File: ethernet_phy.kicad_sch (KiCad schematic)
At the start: 24 parts, among them J2 RJ45_Abracon_ARJP11A-MASA-B-A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, U1 RTL8201F

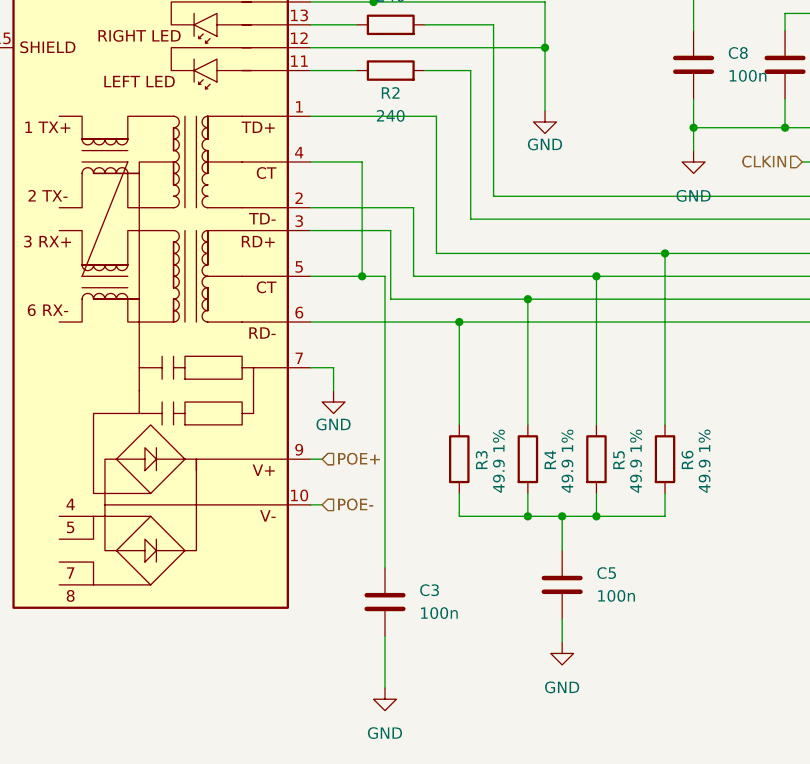
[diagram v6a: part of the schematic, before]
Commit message: RT9400 module option added
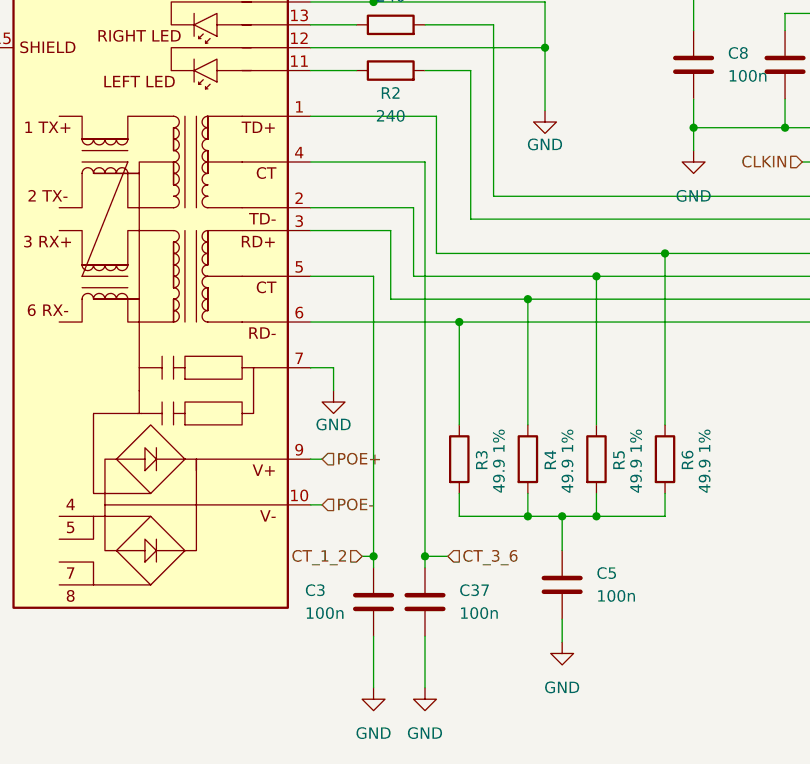
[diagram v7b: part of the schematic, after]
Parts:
- added C37: 100n, Capacitor_SMD:C_0603_1608Metric_Pad1.08x0.95mm_HandSolder, symbol Device:C
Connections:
- net GND: now also C37.2
- net CT_1_2: now reaches C3.1, J2.5 (CT)
- net CT_1_2: no longer J2.4 (CT)
- new net CT_3_6: C37.1, J2.4 (CT)
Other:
- moved on the sheet: C3
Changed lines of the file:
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@@
   (junction (at 92.075 48.26) (diameter 0) (color 0 0 0 0)
   )
+  (junction (at 92.075 128.905) (diameter 0) (color 0 0 0 0)
+  )
   (junction (at 111.125 124.46) (diameter 0) (color 0 0 0 0)
   )
@@
   (junction (at 118.745 48.26) (diameter 0) (color 0 0 0 0)
   )
+  (junction (at 86.36 128.905) (diameter 0) (color 0 0 0 0)
+  )
   (junction (at 107.315 124.46) (diameter 0) (color 0 0 0 0)
   )
@@
   (junction (at 134.62 40.005) (diameter 0) (color 0 0 0 0)
   )
-  (junction (at 85.09 97.79) (diameter 0) (color 0 0 0 0)
-  )
   (junction (at 121.92 81.28) (diameter 0) (color 0 0 0 0)
   )
@@
     (stroke (width 0) (type default) (color 0 0 0 0))
   )
+  (wire (pts (xy 92.075 130.175) (xy 92.075 128.905))
+    (stroke (width 0) (type default) (color 0 0 0 0))
+  )
   (wire (pts (xy 137.16 58.42) (xy 139.065 58.42))
     (stroke (width 0) (type default) (color 0 0 0 0))
@@
     (stroke (width 0) (type default) (color 0 0 0 0))
   )
-  (wire (pts (xy 87.63 137.795) (xy 87.63 143.51))
+  (wire (pts (xy 86.36 137.795) (xy 86.36 143.51))
     (stroke (width 0) (type default) (color 0 0 0 0))
   )
@@
     (stroke (width 0) (type default) (color 0 0 0 0))
   )
+  (wire (pts (xy 92.075 128.905) (xy 94.615 128.905))
+    (stroke (width 0) (type default) (color 0 0 0 0))
+  )
   (wire (pts (xy 107.315 135.89) (xy 107.315 138.43))
     (stroke (width 0) (type default) (color 0 0 0 0))
@@
     (stroke (width 0) (type default) (color 0 0 0 0))
   )
+  (wire (pts (xy 90.805 97.79) (xy 111.125 97.79))
+    (stroke (width 0) (type default) (color 0 0 0 0))
+  )
   (wire (pts (xy 79.375 92.71) (xy 88.265 92.71))
     (stroke (width 0) (type default) (color 0 0 0 0))
@@
     (stroke (width 0) (type default) (color 0 0 0 0))
   )
+  (wire (pts (xy 92.075 128.905) (xy 92.075 85.09))
+    (stroke (width 0) (type default) (color 0 0 0 0))
+  )
   (wire (pts (xy 139.065 64.77) (xy 121.92 64.77))
     (stroke (width 0) (type default) (color 0 0 0 0))
   )
-  (wire (pts (xy 85.09 85.09) (xy 85.09 97.79))
+  (wire (pts (xy 92.075 137.795) (xy 92.075 143.51))
     (stroke (width 0) (type default) (color 0 0 0 0))
   )
@@
     (stroke (width 0) (type default) (color 0 0 0 0))
   )
-  (wire (pts (xy 90.805 97.79) (xy 111.125 97.79))
-    (stroke (width 0) (type default) (color 0 0 0 0))
-  )
   (wire (pts (xy 67.31 58.42) (xy 67.31 55.88))
     (stroke (width 0) (type default) (color 0 0 0 0))
@@
     (stroke (width 0) (type default) (color 0 0 0 0))
   )
-  (wire (pts (xy 87.63 97.79) (xy 87.63 130.175))
-    (stroke (width 0) (type default) (color 0 0 0 0))
-  )
-  (wire (pts (xy 87.63 97.79) (xy 85.09 97.79))
+  (wire (pts (xy 86.36 97.79) (xy 86.36 128.905))
     (stroke (width 0) (type default) (color 0 0 0 0))
   )
@@
     (stroke (width 0) (type default) (color 0 0 0 0))
   )
-  (wire (pts (xy 79.375 97.79) (xy 85.09 97.79))
+  (wire (pts (xy 79.375 97.79) (xy 86.36 97.79))
     (stroke (width 0) (type default) (color 0 0 0 0))
   )
@@
     (stroke (width 0) (type default) (color 0 0 0 0))
   )
+  (wire (pts (xy 86.36 128.905) (xy 86.36 130.175))
+    (stroke (width 0) (type default) (color 0 0 0 0))
+  )
   (wire (pts (xy 177.165 67.31) (xy 193.675 67.31))
     (stroke (width 0) (type default) (color 0 0 0 0))
@@
     (stroke (width 0) (type default) (color 0 0 0 0))
   )
-  (wire (pts (xy 79.375 85.09) (xy 85.09 85.09))
+  (wire (pts (xy 79.375 85.09) (xy 92.075 85.09))
     (stroke (width 0) (type default) (color 0 0 0 0))
   )
@@
   )
   (wire (pts (xy 118.745 95.25) (xy 139.065 95.25))
+    (stroke (width 0) (type default) (color 0 0 0 0))
+  )
+  (wire (pts (xy 85.09 128.905) (xy 86.36 128.905))
     (stroke (width 0) (type default) (color 0 0 0 0))
   )
@@
     (effects (font (size 1.27 1.27)) (justify left))
   )
+  (hierarchical_label "CT_3_6" (shape input) (at 94.615 128.905 0)
+    (effects (font (size 1.27 1.27)) (justify left))
+  )
   (hierarchical_label "EMAC_TX_EN" (shape input) (at 193.675 63.5 0)
     (effects (font (size 1.27 1.27)) (justify left))
@@
   (hierarchical_label "EMAC_RXD0" (shape input) (at 193.675 67.31 0)
     (effects (font (size 1.27 1.27)) (justify left))
+  )
+  (hierarchical_label "CT_1_2" (shape input) (at 85.09 128.905 180)
+    (effects (font (size 1.27 1.27)) (justify right))
   )
   (hierarchical_label "CLKIN" (shape input) (at 133.985 85.09 180)
@@
     (pin "2")
   )
+  (symbol (lib_id "Device:C") (at 92.075 133.985 0) (unit 1)
+    (in_bom yes) (on_board yes)
+    (property "Reference" "C37" (id 0) (at 95.885 132.7149 0)
+      (effects (font (size 1.27 1.27)) (justify left))
+    )
+    (property "Value" "100n" (id 1) (at 95.885 135.2549 0)
+      (effects (font (size 1.27 1.27)) (justify left))
+    )
+    (property "Footprint" "Capacitor_SMD:C_0603_1608Metric_Pad1.08x0.95mm_HandSolder" (id 2) (at 93.0402 137.795 0)
+      (effects (font (size 1.27 1.27)) hide)
+    )
+    (property "Datasheet" "~" (id 3) (at 92.075 133.985 0)
+      (effects (font (size 1.27 1.27)) hide)
+    )
+    (pin "1")
+    (pin "2")
+  )
   (symbol (lib_id "power:GND") (at 108.585 62.23 0) (unit 1)
     (in_bom yes) (on_board yes)
@@
     )
     (property "Datasheet" "" (id 3) (at 158.115 116.84 0)
+      (effects (font (size 1.27 1.27)) hide)
+    )
+    (pin "1")
+  )
+  (symbol (lib_id "power:GND") (at 92.075 143.51 0) (unit 1)
+    (in_bom yes) (on_board yes) (fields_autoplaced)
+    (property "Reference" "#PWR071" (id 0) (at 92.075 149.86 0)
+      (effects (font (size 1.27 1.27)) hide)
+    )
+    (property "Value" "GND" (id 1) (at 92.075 148.59 0))
+    (property "Footprint" "" (id 2) (at 92.075 143.51 0)
+      (effects (font (size 1.27 1.27)) hide)
+    )
+    (property "Datasheet" "" (id 3) (at 92.075 143.51 0)
       (effects (font (size 1.27 1.27)) hide)
     )
@@
     (pin "2")
   )
-  (symbol (lib_id "Device:C") (at 87.63 133.985 0) (unit 1)
-    (in_bom yes) (on_board yes)
-    (property "Reference" "C3" (id 0) (at 91.44 132.7149 0)
-      (effects (font (size 1.27 1.27)) (justify left))
-    )
-    (property "Value" "100n" (id 1) (at 91.44 135.2549 0)
-      (effects (font (size 1.27 1.27)) (justify left))
-    )
-    (property "Footprint" "Capacitor_SMD:C_0603_1608Metric_Pad1.08x0.95mm_HandSolder" (id 2) (at 88.5952 137.795 0)
-      (effects (font (size 1.27 1.27)) hide)
-    )
-    (property "Datasheet" "~" (id 3) (at 87.63 133.985 0)
+  (symbol (lib_id "Device:C") (at 86.36 133.985 0) (unit 1)
+    (in_bom yes) (on_board yes)
+    (property "Reference" "C3" (id 0) (at 78.74 132.715 0)
+      (effects (font (size 1.27 1.27)) (justify left))
+    )
+    (property "Value" "100n" (id 1) (at 78.74 135.255 0)
+      (effects (font (size 1.27 1.27)) (justify left))
+    )
+    (property "Footprint" "Capacitor_SMD:C_0603_1608Metric_Pad1.08x0.95mm_HandSolder" (id 2) (at 87.3252 137.795 0)
+      (effects (font (size 1.27 1.27)) hide)
+    )
+    (property "Datasheet" "~" (id 3) (at 86.36 133.985 0)
       (effects (font (size 1.27 1.27)) hide)
     )
@@
     (pin "2")
   )
-  (symbol (lib_id "power:GND") (at 87.63 143.51 0) (unit 1)
-    (in_bom yes) (on_board yes) (fields_autoplaced)
-    (property "Reference" "#PWR012" (id 0) (at 87.63 149.86 0)
-      (effects (font (size 1.27 1.27)) hide)
-    )
-    (property "Value" "GND" (id 1) (at 87.63 148.59 0))
-    (property "Footprint" "" (id 2) (at 87.63 143.51 0)
-      (effects (font (size 1.27 1.27)) hide)
-    )
-    (property "Datasheet" "" (id 3) (at 87.63 143.51 0)
-      (effects (font (size 1.27 1.27)) hide)
-    )
+  (symbol (lib_id "power:GND") (at 86.36 143.51 0) (unit 1)
+    (in_bom yes) (on_board yes) (fields_autoplaced)
+    (property "Reference" "#PWR012" (id 0) (at 86.36 149.86 0)
+      (effects (font (size 1.27 1.27)) hide)
+    )
+    (property "Value" "GND" (id 1) (at 86.36 148.59 0))
+    (property "Footprint" "" (id 2) (at 86.36 143.51 0)
+      (effects (font (size 1.27 1.27)) hide)
+    )
+    (property "Datasheet" "" (id 3) (at 86.36 143.51 0)
+      (effects (font (size 1.27 1.27)) hide)
+    )

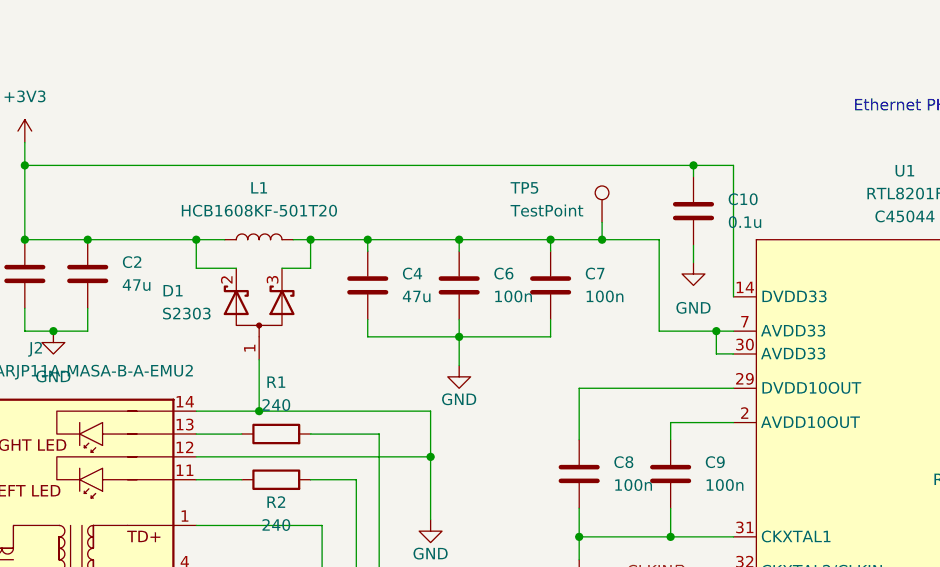
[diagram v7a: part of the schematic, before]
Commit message: Fixup diode footprint and add more LCSC numbers
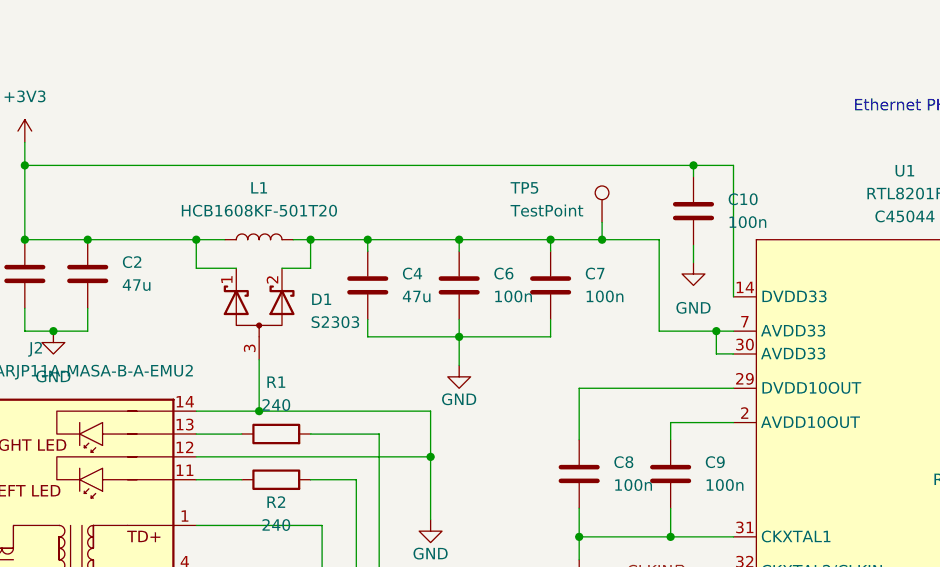
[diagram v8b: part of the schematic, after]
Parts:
- removed D1: S2303, Package_TO_SOT_SMD:TSOT-23_HandSoldering, symbol Device:D_Schottky_Dual_CommonAnode_AKK_Parallel
- added D1: S2303, Package_TO_SOT_SMD:TSOT-23_HandSoldering, symbol Device:D_Schottky_Dual_CommonAnode_KKA_Parallel
- C1, C2, C4: LCSC (none) -> C140782
- C10: value 0.1u -> 100n; LCSC (none) -> C282519
- C3, C37, C5, C6, C7, C8, C9: LCSC (none) -> C282519
- R4, R5, R6: LCSC (none) -> C114625
- R7, R9: LCSC (none) -> C2930027
- R8: LCSC (none) -> C100897
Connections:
- net +3V3: now also D1.1 (K)
- net GND: now also D1.3 (A)
- net at C4.1, C6.1, C7.1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: now also D1.2 (K)
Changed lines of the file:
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@@
       (effects (font (size 1.27 1.27)) hide)
     )
-    (pin "1")
-    (pin "2")
-  )
-  (symbol (lib_id "Device:D_Schottky_Dual_CommonAnode_AKK_Parallel") (at 86.36 56.515 90) (unit 1)
-    (in_bom yes) (on_board yes)
-    (property "Reference" "D1" (id 0) (at 75.565 53.975 90)
-      (effects (font (size 1.27 1.27)) (justify right))
-    )
-    (property "Value" "S2303" (id 1) (at 75.565 56.515 90)
-      (effects (font (size 1.27 1.27)) (justify right))
-    )
-    (property "Footprint" "Package_TO_SOT_SMD:TSOT-23_HandSoldering" (id 2) (at 86.36 57.785 0)
-      (effects (font (size 1.27 1.27)) hide)
-    )
-    (property "Datasheet" "~" (id 3) (at 86.36 57.785 0)
-      (effects (font (size 1.27 1.27)) hide)
-    )
-    (pin "1")
-    (pin "2")
-    (pin "3")
+    (property "LCSC" "C282519" (id 4) (at 108.585 53.34 0)
+      (effects (font (size 1.27 1.27)) hide)
+    )
+    (pin "1")
+    (pin "2")
   )
   (symbol (lib_id "Device:R") (at 88.265 69.85 90) (unit 1)
@@
       (effects (font (size 1.27 1.27)) hide)
     )
+    (property "LCSC" "C2930027" (id 4) (at 188.595 40.005 0)
+      (effects (font (size 1.27 1.27)) hide)
+    )
     (pin "1")
     (pin "2")
@@
       (effects (font (size 1.27 1.27)) hide)
     )
+    (property "LCSC" "C2930027" (id 4) (at 180.975 40.005 0)
+      (effects (font (size 1.27 1.27)) hide)
+    )
     (pin "1")
     (pin "2")
@@
       (effects (font (size 1.27 1.27)) hide)
     )
+    (property "LCSC" "C114625" (id 4) (at 103.505 118.11 90)
+      (effects (font (size 1.27 1.27)) hide)
+    )
     (pin "1")
     (pin "2")
@@
     )
     (property "Datasheet" "~" (id 3) (at 107.315 132.08 0)
+      (effects (font (size 1.27 1.27)) hide)
+    )
+    (property "LCSC" "C282519" (id 4) (at 107.315 132.08 0)
       (effects (font (size 1.27 1.27)) hide)
     )
@@
       (effects (font (size 1.27 1.27)) (justify left))
     )
-    (property "Value" "0.1u" (id 1) (at 138.43 46.3549 0)
+    (property "Value" "100n" (id 1) (at 138.43 46.3549 0)
       (effects (font (size 1.27 1.27)) (justify left))
     )
@@
       (effects (font (size 1.27 1.27)) hide)
     )
+    (property "LCSC" "C282519" (id 4) (at 134.62 45.085 0)
+      (effects (font (size 1.27 1.27)) hide)
+    )
     (pin "1")
     (pin "2")
@@
     )
     (property "Datasheet" "~" (id 3) (at 118.745 118.11 0)
+      (effects (font (size 1.27 1.27)) hide)
+    )
+    (property "LCSC" "C114625" (id 4) (at 118.745 118.11 90)
       (effects (font (size 1.27 1.27)) hide)
     )
@@
       (effects (font (size 1.27 1.27)) hide)
     )
+    (property "LCSC" "C140782" (id 4) (at 67.31 52.07 0)
+      (effects (font (size 1.27 1.27)) hide)
+    )
     (pin "1")
     (pin "2")
@@
     )
     (property "Datasheet" "~" (id 3) (at 118.745 53.34 0)
+      (effects (font (size 1.27 1.27)) hide)
+    )
+    (property "LCSC" "C282519" (id 4) (at 118.745 53.34 0)
       (effects (font (size 1.27 1.27)) hide)
     )
@@
       (effects (font (size 1.27 1.27)) hide)
     )
+    (property "LCSC" "C282519" (id 4) (at 92.075 133.985 0)
+      (effects (font (size 1.27 1.27)) hide)
+    )
     (pin "1")
     (pin "2")
@@
       (effects (font (size 1.27 1.27)) hide)
     )
+    (property "LCSC" "C282519" (id 4) (at 132.08 74.295 0)
+      (effects (font (size 1.27 1.27)) hide)
+    )
     (pin "1")
     (pin "2")
@@
       (effects (font (size 1.27 1.27)) hide)
     )
+    (property "LCSC" "C114625" (id 4) (at 111.125 118.11 90)
+      (effects (font (size 1.27 1.27)) hide)
+    )
     (pin "1")
     (pin "2")
@@
       (effects (font (size 1.27 1.27)) hide)
     )
+    (property "LCSC" "C282519" (id 4) (at 86.36 133.985 0)
+      (effects (font (size 1.27 1.27)) hide)
+    )
     (pin "1")
     (pin "2")
@@
       (effects (font (size 1.27 1.27)) hide)
     )
+    (property "LCSC" "C140782" (id 4) (at 60.325 52.07 0)
+      (effects (font (size 1.27 1.27)) hide)
+    )
     (pin "1")
     (pin "2")
@@
     )
     (property "Datasheet" "~" (id 3) (at 98.425 53.34 0)
+      (effects (font (size 1.27 1.27)) hide)
+    )
+    (property "LCSC" "C140782" (id 4) (at 98.425 53.34 0)
       (effects (font (size 1.27 1.27)) hide)
     )
@@
       (effects (font (size 1.27 1.27)) hide)
     )
+    (property "LCSC" "C100897" (id 4) (at 184.785 115.57 0)
+      (effects (font (size 1.27 1.27)) hide)
+    )
     (pin "1")
     (pin "2")
@@
     (pin "1")
   )
+  (symbol (lib_id "Device:D_Schottky_Dual_CommonAnode_KKA_Parallel") (at 86.36 56.515 90) (unit 1)
+    (in_bom yes) (on_board yes) (fields_autoplaced)
+    (property "Reference" "D1" (id 0) (at 92.075 54.9274 90)
+      (effects (font (size 1.27 1.27)) (justify right))
+    )
+    (property "Value" "S2303" (id 1) (at 92.075 57.4674 90)
+      (effects (font (size 1.27 1.27)) (justify right))
+    )
+    (property "Footprint" "Package_TO_SOT_SMD:TSOT-23_HandSoldering" (id 2) (at 86.36 57.785 0)
+      (effects (font (size 1.27 1.27)) hide)
+    )
+    (property "Datasheet" "https://www.smc-diodes.com/propdf/S2303%20THRU%20S2336%20N0291%20REV.B.pdf" (id 3) (at 86.36 57.785 0)
+      (effects (font (size 1.27 1.27)) hide)
+    )
+    (pin "1")
+    (pin "2")
+    (pin "3")
+  )
   (symbol (lib_id "power:GND") (at 81.915 110.49 0) (unit 1)
     (in_bom yes) (on_board yes)
@@
       (effects (font (size 1.27 1.27)) hide)
     )
+    (property "LCSC" "C282519" (id 4) (at 121.92 74.295 0)
+      (effects (font (size 1.27 1.27)) hide)
+    )
